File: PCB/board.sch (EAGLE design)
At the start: 11 parts, among them Q1 16 MHz, U1 ATMEGA16U2AU

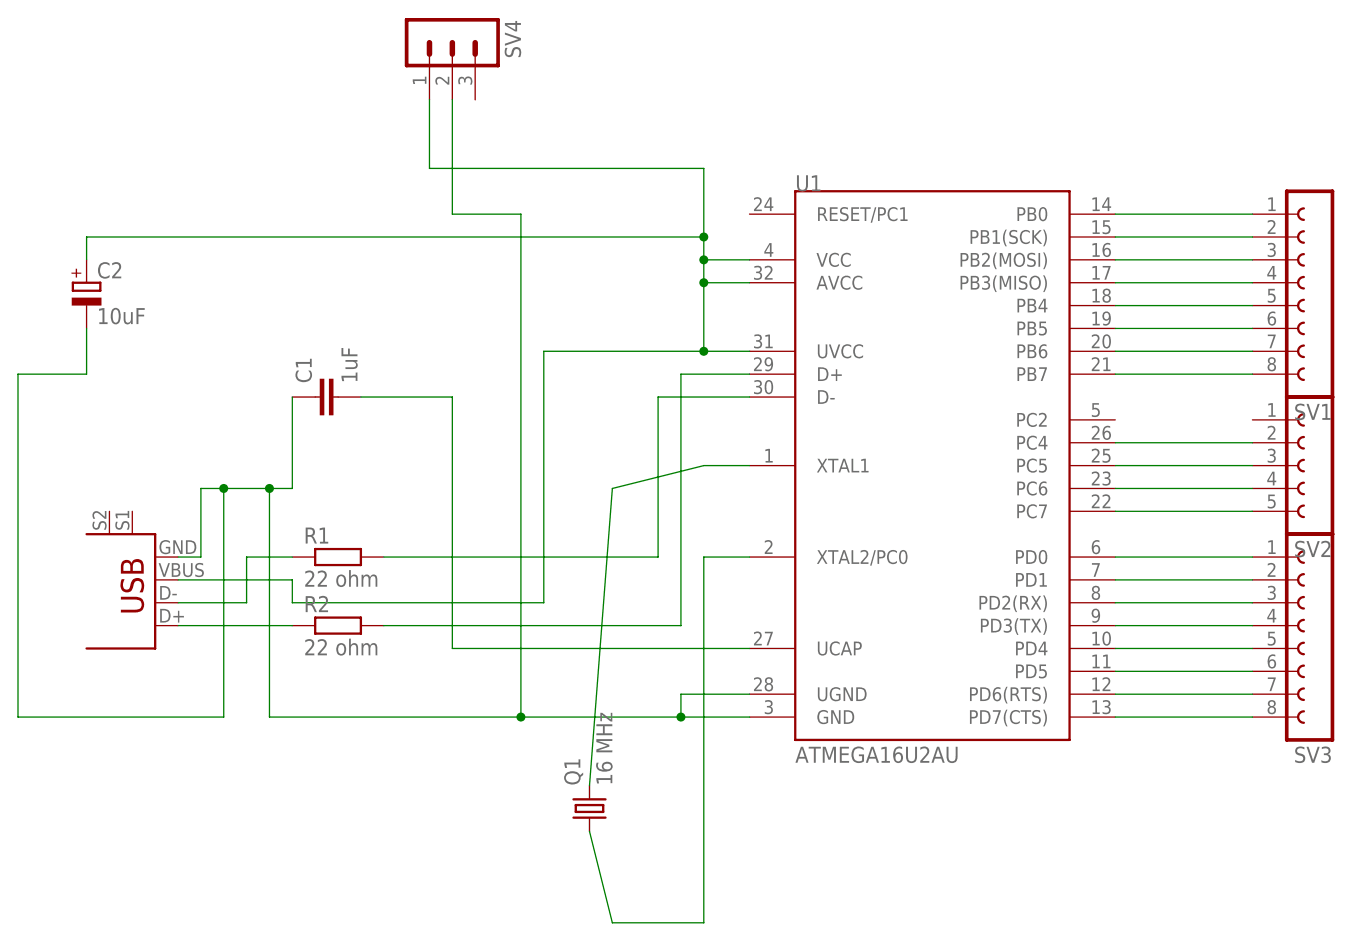
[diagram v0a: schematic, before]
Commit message: fixed PCB design
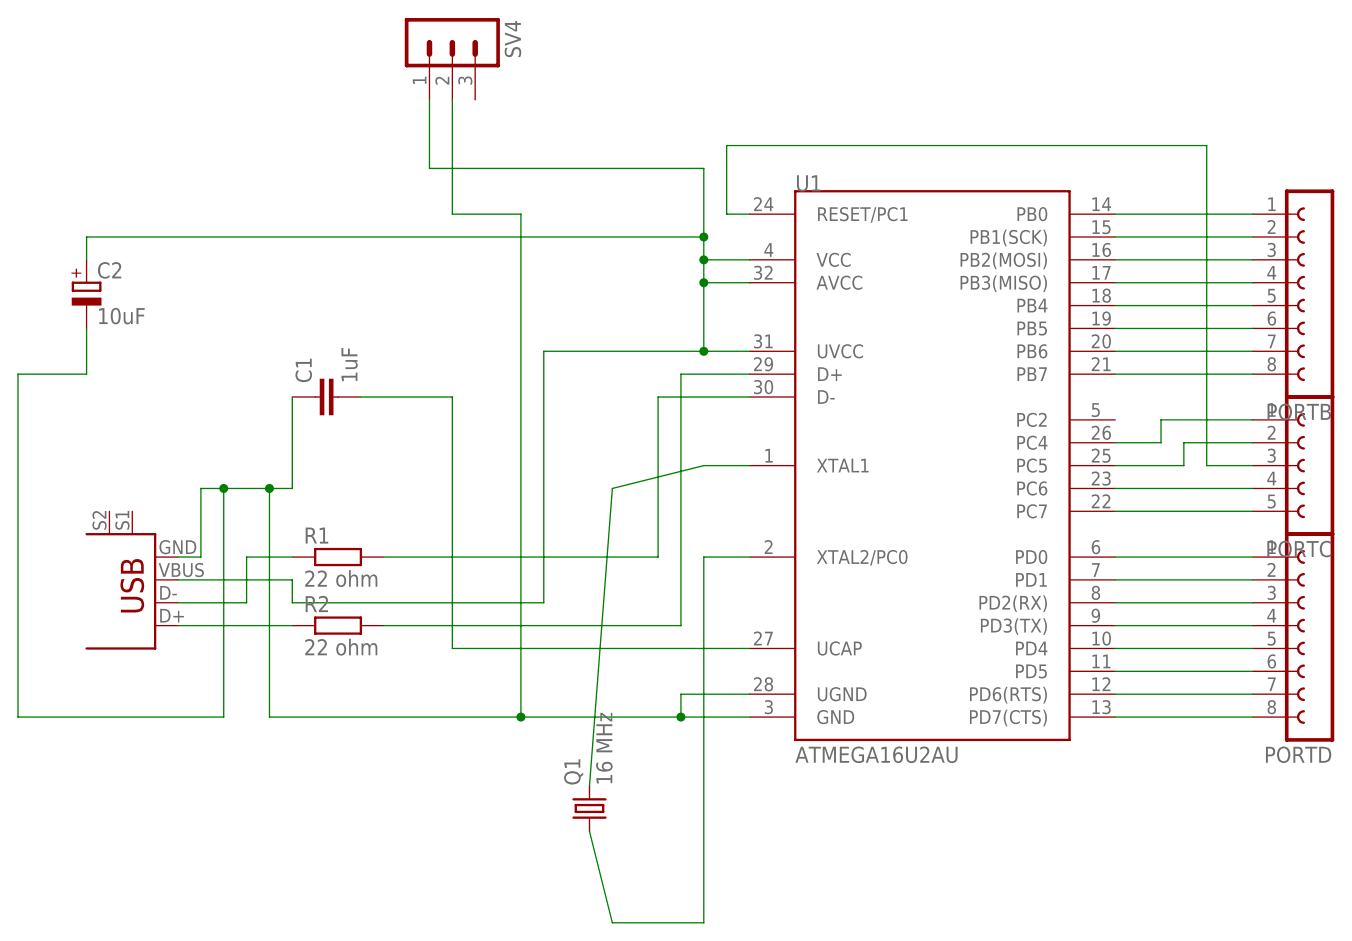
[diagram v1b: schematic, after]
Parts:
- R1, R2: device resistor:R-EU_R0603 -> rcl:R-EU_0207/5V
- renumbered SV1 to PORTB, SV2 to PORTC, SV3 to PORTD
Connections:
- new net N$33: PORTC.3, U1.RESET/PC1
- net N$19: now also U1.PC5; no longer U1.PC4
- net N$20: now also PORTC.1, U1.PC4; no longer PORTC.3, U1.PC5
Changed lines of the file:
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@@
 <parts>
 <part name="U$2" library="SparkFun" deviceset="USB+SHIELD" device=""/>
-<part name="R1" library="resistor" deviceset="R-EU_" device="R0603" value="22 ohm"/>
-<part name="R2" library="resistor" deviceset="R-EU_" device="R0603" value="22 ohm"/>
+<part name="R1" library="rcl" deviceset="R-EU_" device="0207/5V" value="22 ohm"/>
+<part name="R2" library="rcl" deviceset="R-EU_" device="0207/5V" value="22 ohm"/>
 <part name="Q1" library="crystal" deviceset="CRYSTAL" device="HC49S" value="16 MHz"/>
 <part name="C1" library="rcl" deviceset="C-EU" device="025-024X044" value="1uF"/>
 <part name="C2" library="rcl" deviceset="CPOL-EU" device="E1.8-4" value="10uF"/>
 <part name="U1" library="SparkFun" deviceset="ATMEGA8U2" device="AU" value="ATMEGA16U2AU"/>
-<part name="SV1" library="con-lsta" deviceset="FE08-1" device=""/>
-<part name="SV2" library="con-lsta" deviceset="FE05-1" device=""/>
-<part name="SV3" library="con-lsta" deviceset="FE08-1" device=""/>
+<part name="PORTB" library="con-lsta" deviceset="FE08-1" device=""/>
+<part name="PORTC" library="con-lsta" deviceset="FE05-1" device=""/>
+<part name="PORTD" library="con-lsta" deviceset="FE08-1" device=""/>
 <part name="SV4" library="con-lstb" deviceset="MA03-1" device=""/>
 </parts>
@@
 <instance part="C2" gate="G$1" x="-7.62" y="63.5"/>
 <instance part="U1" gate="G$1" x="86.36" y="43.18"/>
-<instance part="SV1" gate="G$1" x="129.54" y="63.5" rot="R180"/>
-<instance part="SV2" gate="G$1" x="129.54" y="43.18" rot="R180"/>
-<instance part="SV3" gate="G$1" x="129.54" y="25.4" rot="R180"/>
+<instance part="PORTB" gate="G$1" x="129.54" y="63.5" rot="R180"/>
+<instance part="PORTC" gate="G$1" x="129.54" y="43.18" rot="R180"/>
+<instance part="PORTD" gate="G$1" x="129.54" y="25.4" rot="R180"/>
 <instance part="SV4" gate="G$1" x="33.02" y="91.44" rot="R270"/>
 </instances>
@@
 <segment>
 <pinref part="U1" gate="G$1" pin="PB0"/>
-<pinref part="SV1" gate="G$1" pin="1"/>
+<pinref part="PORTB" gate="G$1" pin="1"/>
 <wire x1="106.68" y1="71.12" x2="121.92" y2="71.12" width="0.1524" layer="91"/>
 </segment>
@@
 <net name="N$5" class="0">
 <segment>
-<pinref part="SV1" gate="G$1" pin="2"/>
+<pinref part="PORTB" gate="G$1" pin="2"/>
 <pinref part="U1" gate="G$1" pin="PB1(SCK)"/>
 <wire x1="121.92" y1="68.58" x2="106.68" y2="68.58" width="0.1524" layer="91"/>
@@
 <segment>
 <pinref part="U1" gate="G$1" pin="PB2(MOSI)"/>
-<pinref part="SV1" gate="G$1" pin="3"/>
+<pinref part="PORTB" gate="G$1" pin="3"/>
 <wire x1="106.68" y1="66.04" x2="121.92" y2="66.04" width="0.1524" layer="91"/>
 </segment>
@@
 <net name="N$7" class="0">
 <segment>
-<pinref part="SV1" gate="G$1" pin="4"/>
+<pinref part="PORTB" gate="G$1" pin="4"/>
 <pinref part="U1" gate="G$1" pin="PB3(MISO)"/>
 <wire x1="121.92" y1="63.5" x2="106.68" y2="63.5" width="0.1524" layer="91"/>
@@
 <segment>
 <pinref part="U1" gate="G$1" pin="PB4"/>
-<pinref part="SV1" gate="G$1" pin="5"/>
+<pinref part="PORTB" gate="G$1" pin="5"/>
 <wire x1="106.68" y1="60.96" x2="121.92" y2="60.96" width="0.1524" layer="91"/>
 </segment>
@@
 <net name="N$15" class="0">
 <segment>
-<pinref part="SV1" gate="G$1" pin="6"/>
+<pinref part="PORTB" gate="G$1" pin="6"/>
 <pinref part="U1" gate="G$1" pin="PB5"/>
 <wire x1="121.92" y1="58.42" x2="106.68" y2="58.42" width="0.1524" layer="91"/>
@@
 <segment>
 <pinref part="U1" gate="G$1" pin="PB6"/>
-<pinref part="SV1" gate="G$1" pin="7"/>
+<pinref part="PORTB" gate="G$1" pin="7"/>
 <wire x1="106.68" y1="55.88" x2="121.92" y2="55.88" width="0.1524" layer="91"/>
 </segment>
@@
 <net name="N$17" class="0">
 <segment>
-<pinref part="SV1" gate="G$1" pin="8"/>
+<pinref part="PORTB" gate="G$1" pin="8"/>
 <pinref part="U1" gate="G$1" pin="PB7"/>
 <wire x1="121.92" y1="53.34" x2="106.68" y2="53.34" width="0.1524" layer="91"/>
 </segment>
 </net>
-<net name="N$19" class="0">
-<segment>
-<pinref part="SV2" gate="G$1" pin="2"/>
-<pinref part="U1" gate="G$1" pin="PC4"/>
-<wire x1="121.92" y1="45.72" x2="106.68" y2="45.72" width="0.1524" layer="91"/>
-</segment>
-</net>
-<net name="N$20" class="0">
-<segment>
-<pinref part="U1" gate="G$1" pin="PC5"/>
-<pinref part="SV2" gate="G$1" pin="3"/>
-<wire x1="106.68" y1="43.18" x2="121.92" y2="43.18" width="0.1524" layer="91"/>
-</segment>
-</net>
 <net name="N$21" class="0">
 <segment>
-<pinref part="SV2" gate="G$1" pin="4"/>
+<pinref part="PORTC" gate="G$1" pin="4"/>
 <pinref part="U1" gate="G$1" pin="PC6"/>
 <wire x1="121.92" y1="40.64" x2="106.68" y2="40.64" width="0.1524" layer="91"/>
@@
 <segment>
 <pinref part="U1" gate="G$1" pin="PC7"/>
-<pinref part="SV2" gate="G$1" pin="5"/>
+<pinref part="PORTC" gate="G$1" pin="5"/>
 <wire x1="106.68" y1="38.1" x2="121.92" y2="38.1" width="0.1524" layer="91"/>
 </segment>
@@
 <segment>
 <pinref part="U1" gate="G$1" pin="PD7(CTS)"/>
-<pinref part="SV3" gate="G$1" pin="8"/>
+<pinref part="PORTD" gate="G$1" pin="8"/>
 <wire x1="106.68" y1="15.24" x2="121.92" y2="15.24" width="0.1524" layer="91"/>
 </segment>
@@
 <net name="N$23" class="0">
 <segment>
-<pinref part="SV3" gate="G$1" pin="7"/>
+<pinref part="PORTD" gate="G$1" pin="7"/>
 <pinref part="U1" gate="G$1" pin="PD6(RTS)"/>
 <wire x1="121.92" y1="17.78" x2="106.68" y2="17.78" width="0.1524" layer="91"/>
@@
 <segment>
 <pinref part="U1" gate="G$1" pin="PD5"/>
-<pinref part="SV3" gate="G$1" pin="6"/>
+<pinref part="PORTD" gate="G$1" pin="6"/>
 <wire x1="106.68" y1="20.32" x2="121.92" y2="20.32" width="0.1524" layer="91"/>
 </segment>
@@
 <net name="N$25" class="0">
 <segment>
-<pinref part="SV3" gate="G$1" pin="5"/>
+<pinref part="PORTD" gate="G$1" pin="5"/>
 <pinref part="U1" gate="G$1" pin="PD4"/>
 <wire x1="121.92" y1="22.86" x2="106.68" y2="22.86" width="0.1524" layer="91"/>
@@
 <segment>
 <pinref part="U1" gate="G$1" pin="PD3(TX)"/>
-<pinref part="SV3" gate="G$1" pin="4"/>
+<pinref part="PORTD" gate="G$1" pin="4"/>
 <wire x1="106.68" y1="25.4" x2="121.92" y2="25.4" width="0.1524" layer="91"/>
 </segment>
@@
 <net name="N$27" class="0">
 <segment>
-<pinref part="SV3" gate="G$1" pin="3"/>
+<pinref part="PORTD" gate="G$1" pin="3"/>
 <pinref part="U1" gate="G$1" pin="PD2(RX)"/>
 <wire x1="121.92" y1="27.94" x2="106.68" y2="27.94" width="0.1524" layer="91"/>
@@
 <segment>
 <pinref part="U1" gate="G$1" pin="PD1"/>
-<pinref part="SV3" gate="G$1" pin="2"/>
+<pinref part="PORTD" gate="G$1" pin="2"/>
 <wire x1="106.68" y1="30.48" x2="121.92" y2="30.48" width="0.1524" layer="91"/>
 </segment>
@@
 <net name="N$29" class="0">
 <segment>
-<pinref part="SV3" gate="G$1" pin="1"/>
+<pinref part="PORTD" gate="G$1" pin="1"/>
 <pinref part="U1" gate="G$1" pin="PD0"/>
 <wire x1="121.92" y1="33.02" x2="106.68" y2="33.02" width="0.1524" layer="91"/>
@@
 </segment>
 </net>
+<net name="N$33" class="0">
+<segment>
+<pinref part="U1" gate="G$1" pin="RESET/PC1"/>
+<wire x1="66.04" y1="71.12" x2="63.5" y2="71.12" width="0.1524" layer="91"/>
+<wire x1="63.5" y1="71.12" x2="63.5" y2="78.74" width="0.1524" layer="91"/>
+<wire x1="63.5" y1="78.74" x2="116.84" y2="78.74" width="0.1524" layer="91"/>
+<wire x1="116.84" y1="78.74" x2="116.84" y2="43.18" width="0.1524" layer="91"/>
+<pinref part="PORTC" gate="G$1" pin="3"/>
+<wire x1="116.84" y1="43.18" x2="121.92" y2="43.18" width="0.1524" layer="91"/>
+</segment>
+</net>
+<net name="N$19" class="0">
+<segment>
+<pinref part="U1" gate="G$1" pin="PC5"/>
+<wire x1="106.68" y1="43.18" x2="114.3" y2="43.18" width="0.1524" layer="91"/>
+<wire x1="114.3" y1="43.18" x2="114.3" y2="45.72" width="0.1524" layer="91"/>
+<pinref part="PORTC" gate="G$1" pin="2"/>
+<wire x1="114.3" y1="45.72" x2="121.92" y2="45.72" width="0.1524" layer="91"/>
+</segment>
+</net>
+<net name="N$20" class="0">
+<segment>
+<pinref part="U1" gate="G$1" pin="PC4"/>
+<wire x1="106.68" y1="45.72" x2="111.76" y2="45.72" width="0.1524" layer="91"/>
+<wire x1="111.76" y1="45.72" x2="111.76" y2="48.26" width="0.1524" layer="91"/>
+<pinref part="PORTC" gate="G$1" pin="1"/>
+<wire x1="111.76" y1="48.26" x2="121.92" y2="48.26" width="0.1524" layer="91"/>
+</segment>
+</net>
